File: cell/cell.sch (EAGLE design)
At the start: 11 parts

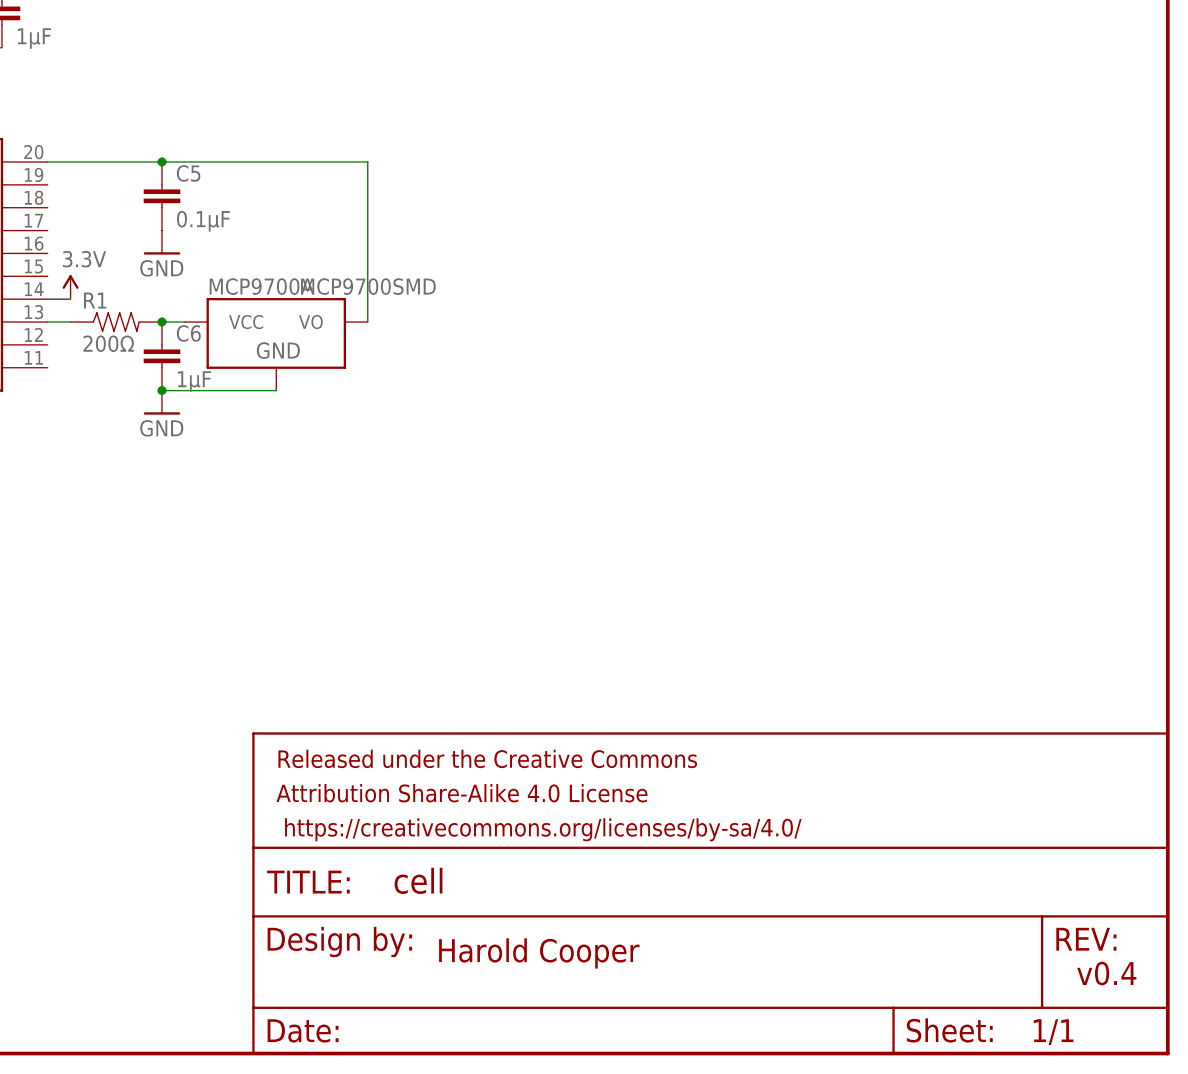
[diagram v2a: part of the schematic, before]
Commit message: replace MCP9700A with LMT70
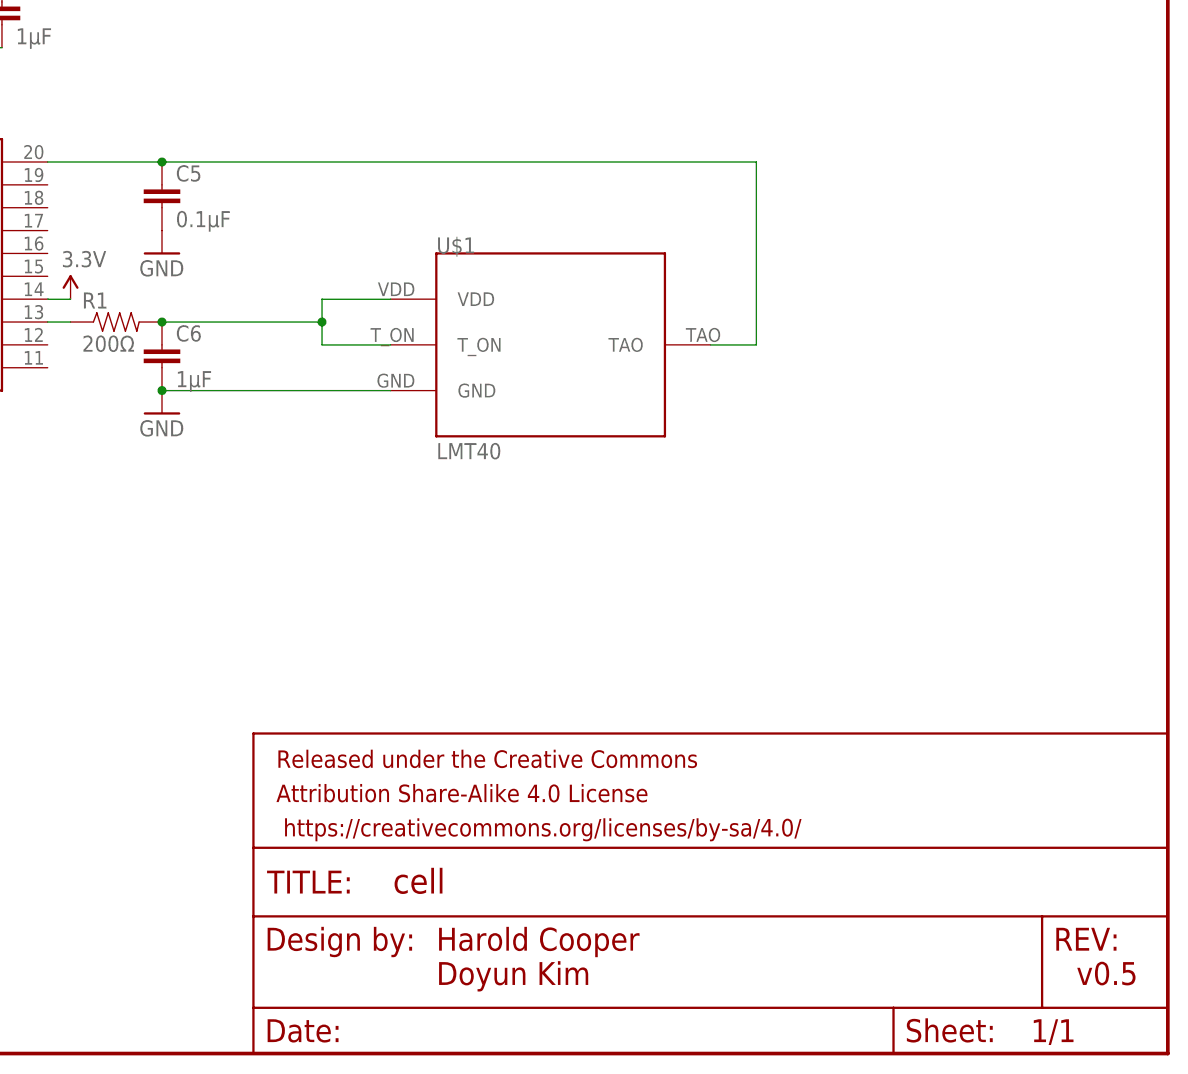
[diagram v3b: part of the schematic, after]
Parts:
- removed MCP9700A: MCP9700SMD, SparkFun-Sensors:MCP9700SMD
- added U$1: LMT40, lmt40:LMT40
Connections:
- removed net N$3: C5.1, MCP9700A.VO, XB24.DIO0
- new net N$7: C5.1, U$1.TAO, XB24.DIO0
- net GND: now also U$1.GND; no longer MCP9700A.GND
- net N$1: now also U$1.T_ON, U$1.VDD; no longer MCP9700A.VCC
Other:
- note added: "Harold Cooper Doyun Kim"
- note added: "v0.5"
- note removed: "Harold Cooper"
- note removed: "v0.4"
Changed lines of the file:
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@@
 <?xml version="1.0" encoding="utf-8"?>
 <!DOCTYPE eagle SYSTEM "eagle.dtd">
-<eagle version="7.1.0">
+<eagle version="7.3.0">
 <drawing>
 <settings>
@@
 <part name="MCP1700" library="hrldcpr" deviceset="MCP1700" device=""/>
 <part name="C2" library="SparkFun-Capacitors" deviceset="CAP" device="0805" value="1µF"/>
-<part name="MCP9700A" library="SparkFun-Sensors" deviceset="MCP9700" device="SMD"/>
 <part name="XB24" library="hrldcpr" deviceset="XBEE-1" device="XBEE-1"/>
+<part name="U$1" library="lmt40" deviceset="LMT40" device=""/>
 </parts>
 <sheets>
 <sheet>
 <plain>
-<text x="167.64" y="10.16" size="2.54" layer="94">Harold Cooper</text>
-<text x="238.76" y="7.62" size="2.54" layer="94">v0.4</text>
+<text x="167.64" y="7.62" size="2.54" layer="94">Harold Cooper
+Doyun Kim</text>
+<text x="238.76" y="7.62" size="2.54" layer="94">v0.5</text>
 </plain>
 <instances>
@@
 <instance part="MCP1700" gate="G$1" x="104.14" y="119.38"/>
 <instance part="C2" gate="G$1" x="119.38" y="114.3"/>
-<instance part="MCP9700A" gate="G$1" x="149.86" y="78.74"/>
 <instance part="XB24" gate="G$1" x="104.14" y="88.9"/>
+<instance part="U$1" gate="G$1" x="180.34" y="78.74"/>
 </instances>
 <busses>
@@
 <pinref part="C6" gate="G$1" pin="2"/>
 <junction x="137.16" y="73.66"/>
-<pinref part="MCP9700A" gate="G$1" pin="GND"/>
-<wire x1="137.16" y1="73.66" x2="149.86" y2="73.66" width="0.1524" layer="91"/>
+<pinref part="U$1" gate="G$1" pin="GND"/>
+<wire x1="137.16" y1="73.66" x2="162.56" y2="73.66" width="0.1524" layer="91"/>
 </segment>
 <segment>
@@
 <pinref part="C6" gate="G$1" pin="1"/>
 <pinref part="R1" gate="G$1" pin="2"/>
-<pinref part="MCP9700A" gate="G$1" pin="VCC"/>
-<pinref part="MCP9700A" gate="G$1" pin="VCC"/>
-<wire x1="139.7" y1="81.28" x2="137.16" y2="81.28" width="0.1524" layer="91"/>
 <junction x="137.16" y="81.28"/>
+<wire x1="137.16" y1="81.28" x2="154.94" y2="81.28" width="0.1524" layer="91"/>
+<wire x1="154.94" y1="81.28" x2="154.94" y2="83.82" width="0.1524" layer="91"/>
+<pinref part="U$1" gate="G$1" pin="VDD"/>
+<wire x1="154.94" y1="83.82" x2="162.56" y2="83.82" width="0.1524" layer="91"/>
+<pinref part="U$1" gate="G$1" pin="T_ON"/>
+<wire x1="162.56" y1="78.74" x2="154.94" y2="78.74" width="0.1524" layer="91"/>
+<wire x1="154.94" y1="78.74" x2="154.94" y2="81.28" width="0.1524" layer="91"/>
+<junction x="154.94" y="81.28"/>
 </segment>
 </net>
@@
 </segment>
 </net>
-<net name="N$3" class="0">
+<net name="N$7" class="0">
 <segment>
 <pinref part="C5" gate="G$1" pin="1"/>
 <wire x1="137.16" y1="99.06" x2="124.46" y2="99.06" width="0.1524" layer="91"/>
+<pinref part="XB24" gate="G$1" pin="DIO0"/>
+<pinref part="U$1" gate="G$1" pin="TAO"/>
+<wire x1="198.12" y1="78.74" x2="203.2" y2="78.74" width="0.1524" layer="91"/>
+<wire x1="203.2" y1="78.74" x2="203.2" y2="99.06" width="0.1524" layer="91"/>
+<wire x1="137.16" y1="99.06" x2="203.2" y2="99.06" width="0.1524" layer="91"/>
 <junction x="137.16" y="99.06"/>
-<pinref part="MCP9700A" gate="G$1" pin="VO"/>
-<wire x1="160.02" y1="81.28" x2="160.02" y2="99.06" width="0.1524" layer="91"/>
-<wire x1="160.02" y1="99.06" x2="137.16" y2="99.06" width="0.1524" layer="91"/>
-<pinref part="XB24" gate="G$1" pin="DIO0"/>
 </segment>
 </net>
@@
 </sheet>
 </sheets>
+<errors>
+</errors>
 </schematic>
 </drawing>
+<compatibility>
+<note version="6.3" minversion="6.2.2" severity="warning">
+Since Version 6.2.2 text objects can contain more than one line,
+which will not be processed correctly with this version.
+</note>
+</compatibility>
 </eagle>

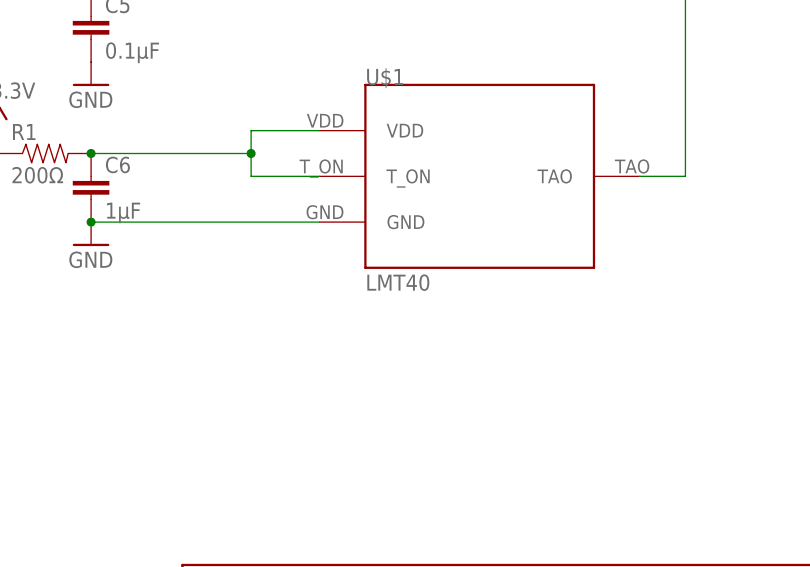
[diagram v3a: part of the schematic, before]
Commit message: fix LMT70 naming
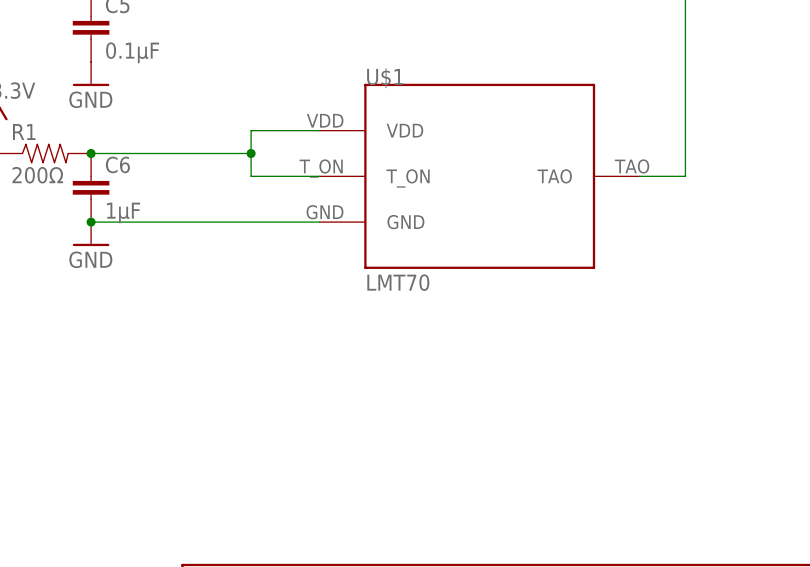
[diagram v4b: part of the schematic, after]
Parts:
- U$1: value LMT40 -> LMT70; device lmt40:LMT40 -> lmt70:LMT70
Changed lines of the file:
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@@
 <part name="C2" library="SparkFun-Capacitors" deviceset="CAP" device="0805" value="1µF"/>
 <part name="XB24" library="hrldcpr" deviceset="XBEE-1" device="XBEE-1"/>
-<part name="U$1" library="lmt40" deviceset="LMT40" device=""/>
+<part name="U$1" library="lmt70" deviceset="LMT70" device=""/>
 </parts>
 <sheets>
